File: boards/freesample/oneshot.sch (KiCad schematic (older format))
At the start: 0 parts

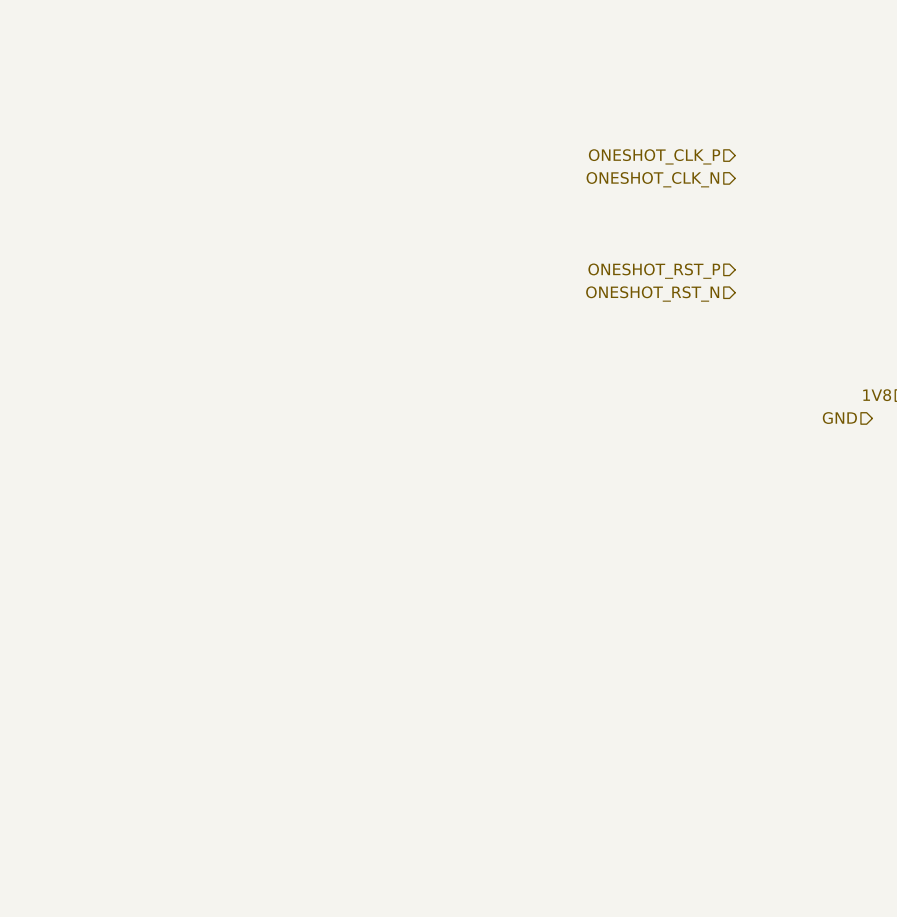
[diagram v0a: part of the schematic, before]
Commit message: Continued initial schematic capture
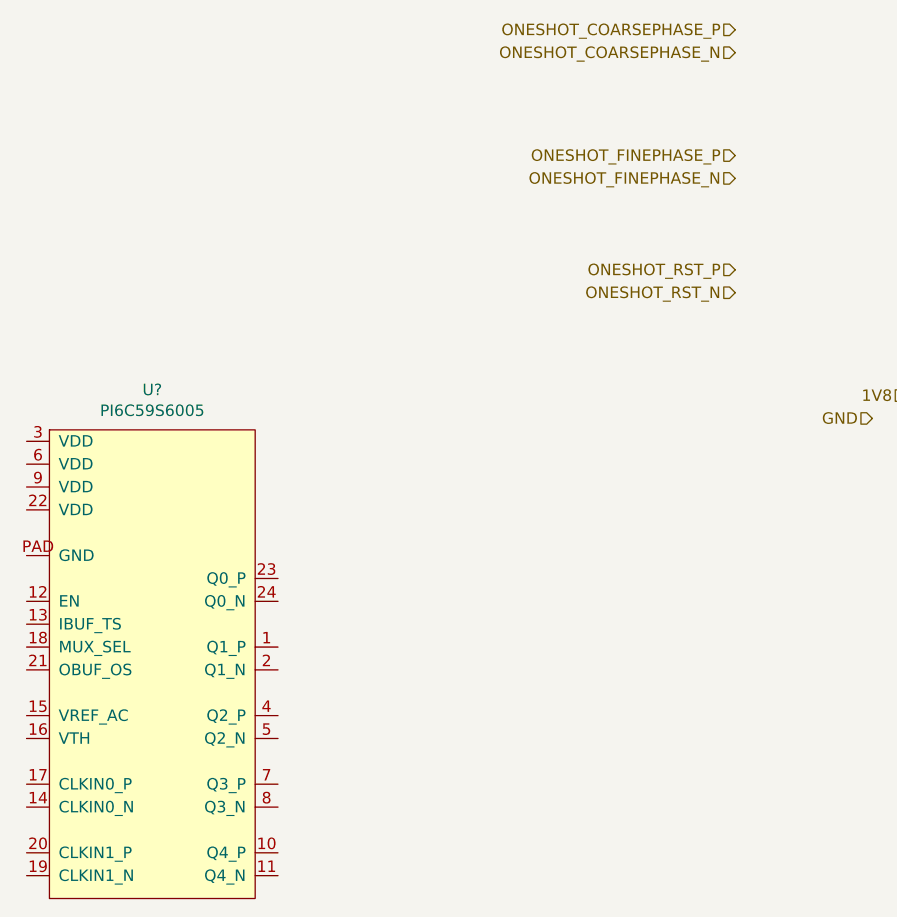
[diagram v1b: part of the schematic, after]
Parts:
- added U?: PI6C59S6005, symbol special-azonenberg:PI6C59S6005
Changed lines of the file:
@@
 $Descr A4 11693 8268
 encoding utf-8
-Sheet 6 11
+Sheet 6 12
 Title "FREESAMPLE Oscilloscope"
-Date "2018-12-15"
+Date "2018-12-17"
 Rev "0.1"
 Comp "Andrew D. Zonenberg / Antikernel Labs"
@@
 ONESHOT_RST_N
 Text HLabel 6150 2150 0    50   Input ~ 0
-ONESHOT_CLK_P
+ONESHOT_FINEPHASE_P
 Text HLabel 6150 2250 0    50   Input ~ 0
-ONESHOT_CLK_N
+ONESHOT_FINEPHASE_N
 Text HLabel 6900 3200 0    50   Input ~ 0
 1V8
@@
 Text HLabel 8450 3250 0    50   Output ~ 0
 ONESHOT_TRIGGERED_N
+$Comp
+L special-azonenberg:PI6C59S6005 U?
+U 1 1 5C3E7E97
+P 3150 5400
+F 0 "U?" H 3600 7625 50  0000 C CNN
+F 1 "PI6C59S6005" H 3600 7534 50  0000 C CNN
+F 2 "" H 3150 5100 50  0001 C CNN
+F 3 "" H 3150 5100 50  0001 C CNN
+	1    3150 5400
+	1    0    0    -1
+$EndComp
+Text HLabel 6150 1600 0    50   Input ~ 0
+ONESHOT_COARSEPHASE_P
+Text HLabel 6150 1700 0    50   Input ~ 0
+ONESHOT_COARSEPHASE_N
 $EndSCHEMATC

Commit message: Continued work on schematic capture
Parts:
- gave numbers to parts that had none: 1
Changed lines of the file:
@@
 Rev "0.1"
 Comp "Andrew D. Zonenberg / Antikernel Labs"
-Comment1 ""
+Comment1 "Digital one-shot and reset sync for ADC trigger"
 Comment2 ""
 Comment3 ""
@@
 ONESHOT_TRIGGERED_N
 $Comp
-L special-azonenberg:PI6C59S6005 U?
+L special-azonenberg:PI6C59S6005 U7
 U 1 1 5C3E7E97
 P 3150 5400
-F 0 "U?" H 3600 7625 50  0000 C CNN
+F 0 "U7" H 3600 7625 50  0000 C CNN
 F 1 "PI6C59S6005" H 3600 7534 50  0000 C CNN
 F 2 "" H 3150 5100 50  0001 C CNN

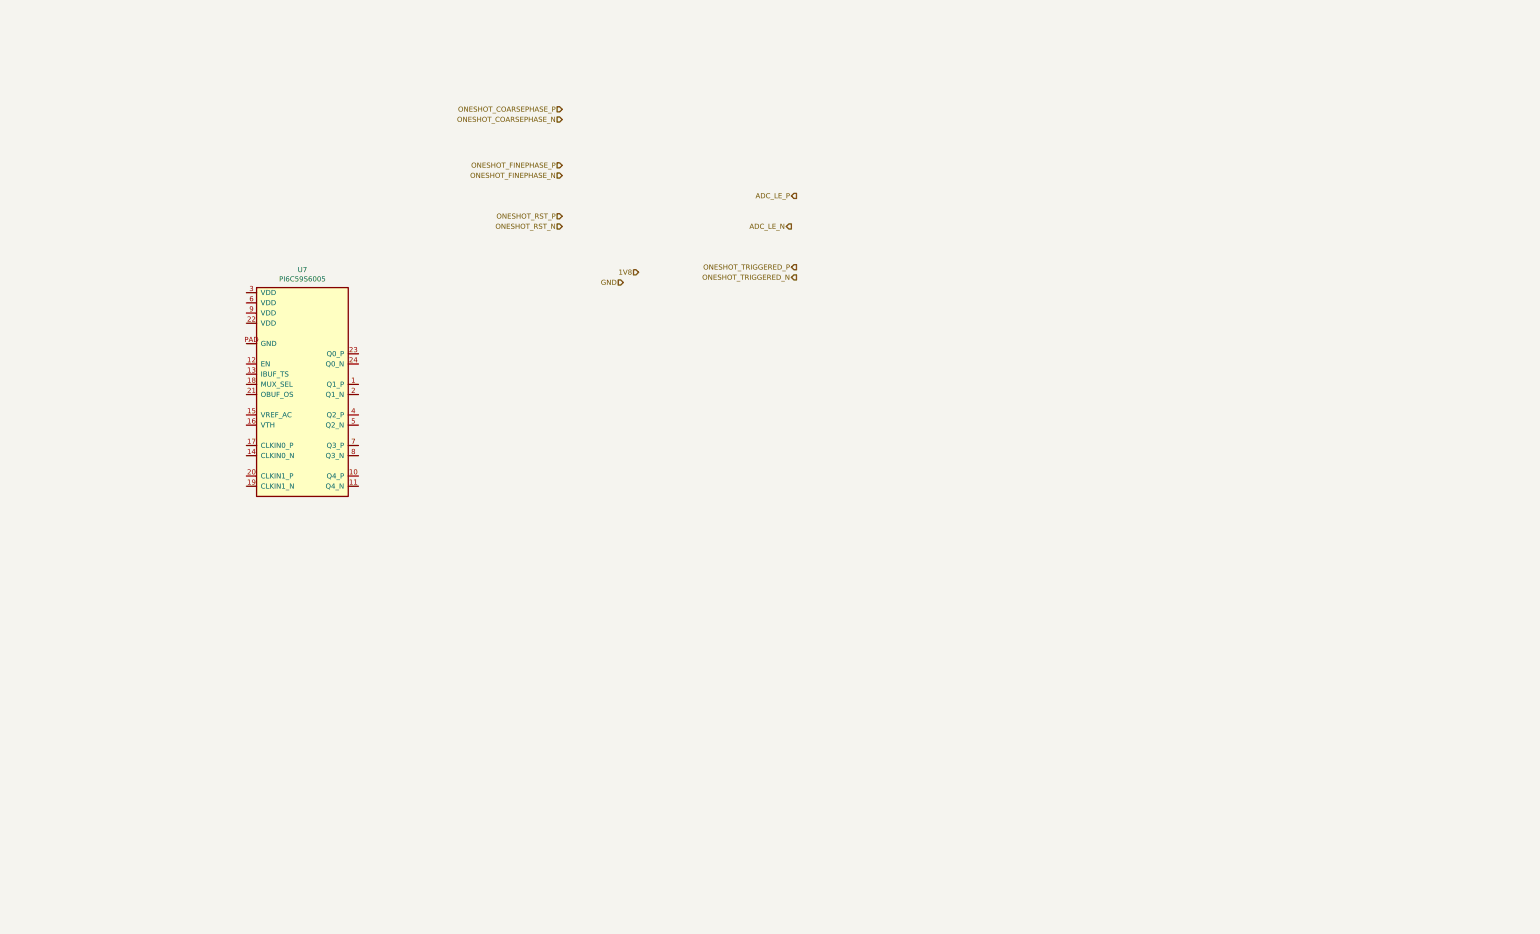
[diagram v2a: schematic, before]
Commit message: Continued work on FREESAMPLE schematic including PSU.
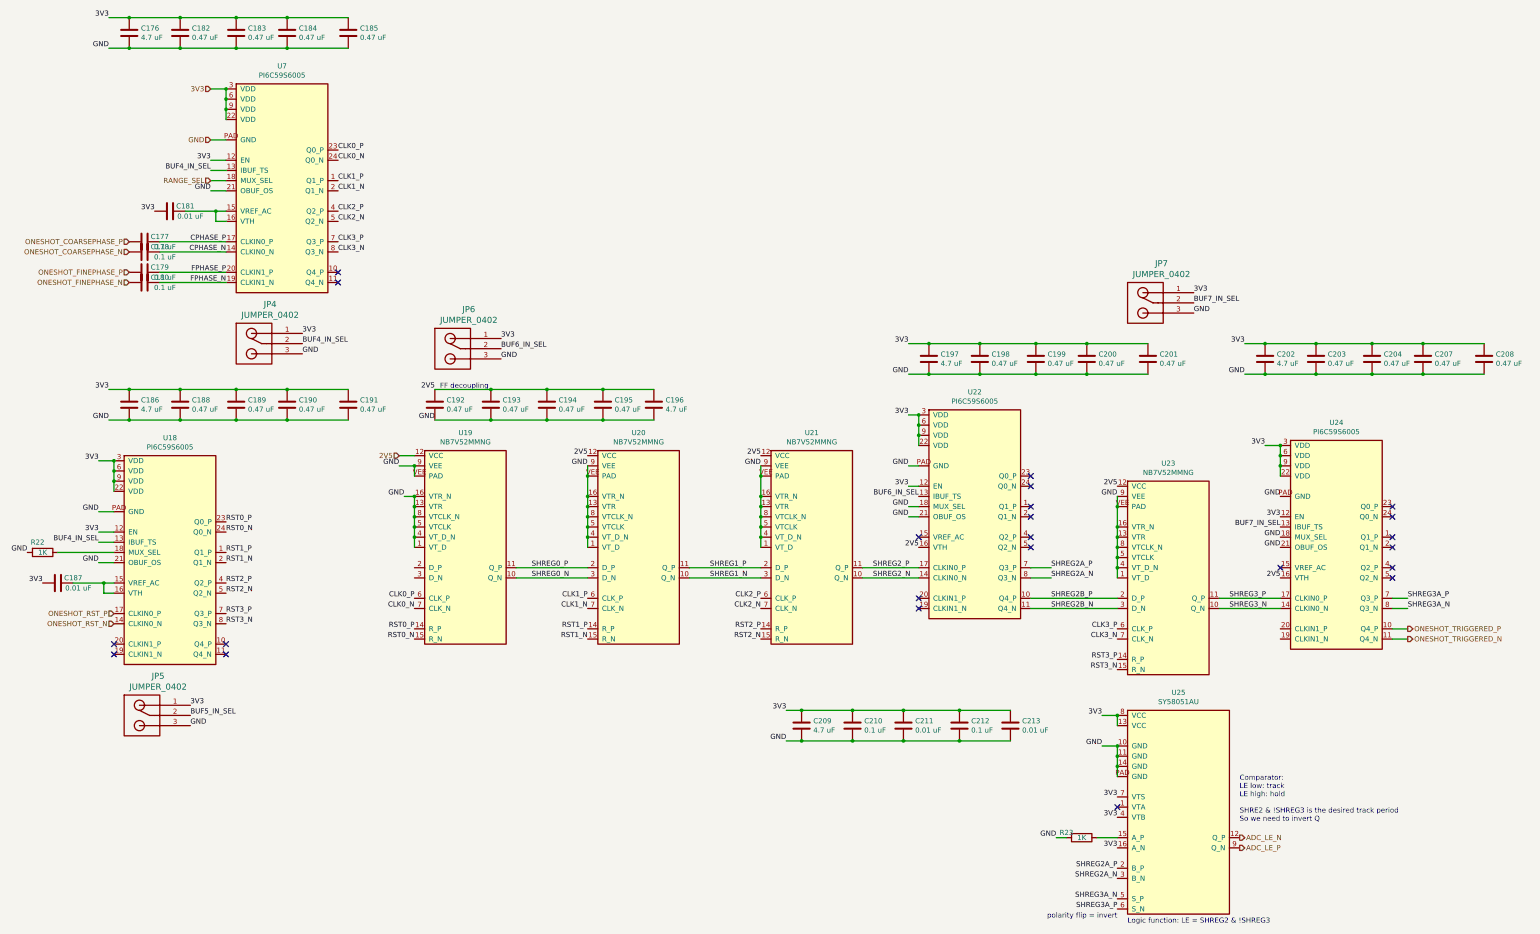
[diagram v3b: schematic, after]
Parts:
- added C176, C186, C196, C197, C202, C209: 4.7 uF, symbol device:C
- added C177, C178, C179, C180, C210, C212: 0.1 uF, symbol device:C
- added C181, C187, C211, C213: 0.01 uF, symbol device:C
- added C182, C183, C184, C185, C188, C189, C190, C191, C192, C193, C194, C195, C198, C199, C200, C201, C203, C204, C207, C208: 0.47 uF, symbol device:C
- added JP4, JP5, JP6, JP7: JUMPER_0402, symbol special-azonenberg:JUMPER_0402_SPDT
- added R22, R23: 1K, symbol device:R
- added U18, U22, U24: PI6C59S6005, symbol special-azonenberg:PI6C59S6005
- added U19, U20, U21, U23: NB7V52MMNG, symbol special-azonenberg:NB7V52MMNG
- added U25: SY58051AU, symbol special-azonenberg:SY58051AU
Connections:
- net ADC_LE_N: now also U25.12 (Q_P)
- net ADC_LE_P: now also U25.9 (Q_N)
- net GND: now also U7.21 (OBUF_OS), U7.PAD (GND), C176.2, C182.2, C183.2, C184.2, C185.2, C186.2, C188.2, C189.2, C190.2, C191.2, C192.2, C193.2, C194.2, C195.2, C196.2, C197.2, C198.2, C199.2, C200.2, C201.2, C202.2, C203.2, C204.2, C207.2, C208.2, C209.2, C210.2, C211.2, C212.2, C213.2, JP4.3, JP5.3, JP6.3, JP7.3, R22.2, R23.2, U18.21 (OBUF_OS), U18.PAD (GND), U19.1 (VT_D), U19.13 (VTR), U19.16 (VTR_N), U19.4 (VT_D_N), U19.5 (VTCLK), U19.8 (VTCLK_N), U19.9 (VEE), U19.VEE (PAD), U20.1 (VT_D), U20.13 (VTR), U20.16 (VTR_N), U20.4 (VT_D_N), U20.5 (VTCLK), U20.8 (VTCLK_N), U20.9 (VEE), U20.VEE (PAD), U21.1 (VT_D), U21.13 (VTR), U21.16 (VTR_N), U21.4 (VT_D_N), U21.5 (VTCLK), U21.8 (VTCLK_N), U21.9 (VEE), U21.VEE (PAD), U22.18 (MUX_SEL), U22.21 (OBUF_OS), U22.PAD (GND), U23.1 (VT_D), U23.13 (VTR), U23.16 (VTR_N), U23.4 (VT_D_N), U23.5 (VTCLK), U23.8 (VTCLK_N), U23.9 (VEE), U23.VEE (PAD), U24.18 (MUX_SEL), U24.21 (OBUF_OS), U24.PAD (GND), U25.10 (GND), U25.11 (GND), U25.14 (GND), U25.PAD (GND)
- net ONESHOT_COARSEPHASE_N: now also C178.2
- net ONESHOT_COARSEPHASE_P: now also C177.2
- net ONESHOT_FINEPHASE_N: now also C180.2
- net ONESHOT_FINEPHASE_P: now also C179.2
- net ONESHOT_RST_N: now also U18.14 (CLKIN0_N)
- net ONESHOT_RST_P: now also U18.17 (CLKIN0_P)
- net ONESHOT_TRIGGERED_N: now also U24.11 (Q4_N)
- net ONESHOT_TRIGGERED_P: now also U24.10 (Q4_P)
- net CLK1_P: now reaches U7.1 (Q1_P)
- net CLK1_P: now also U20.6 (CLK_P)
- net 3V3: now reaches U7.12 (EN)
- net 3V3: now also U7.22 (VDD), U7.3 (VDD), U7.6 (VDD), U7.9 (VDD), C176.1, C181.2, C182.1, C183.1, C184.1, C185.1, C186.1, C187.2, C188.1, C189.1, C190.1, C191.1, C197.1, C198.1, C199.1, C200.1, C201.1, C202.1, C203.1, C204.1, C207.1, C208.1, C209.1, C210.1, C211.1, C212.1, C213.1, JP4.1, JP5.1, JP6.1, JP7.1, U18.12 (EN), U18.22 (VDD), U18.3 (VDD), U18.6 (VDD), U18.9 (VDD), U22.12 (EN), U22.22 (VDD), U22.3 (VDD), U22.6 (VDD), U22.9 (VDD), U24.12 (EN), U24.22 (VDD), U24.3 (VDD), U24.6 (VDD), U24.9 (VDD), U25.13 (VCC), U25.16 (A_N), U25.4 (VTB), U25.7 (VTS), U25.8 (VCC)
- net BUF4_IN_SEL: now reaches U7.13 (IBUF_TS)
- net BUF4_IN_SEL: now also JP4.2, U18.13 (IBUF_TS)
- net CPHASE_N: now reaches U7.14 (CLKIN0_N)
- net CPHASE_N: now also C178.1
- net at U7.15 (VREF_AC): now also U7.16 (VTH), C181.1
- net CPHASE_P: now reaches U7.17 (CLKIN0_P)
- net CPHASE_P: now also C177.1
- net RANGE_SEL: now reaches U7.18 (MUX_SEL)
- net FPHASE_N: now reaches U7.19 (CLKIN1_N)
- net FPHASE_N: now also C180.1
- net CLK1_N: now reaches U7.2 (Q1_N)
- net CLK1_N: now also U20.7 (CLK_N)
- net FPHASE_P: now reaches U7.20 (CLKIN1_P)
- net FPHASE_P: now also C179.1
- net CLK0_P: now reaches U7.23 (Q0_P)
- net CLK0_P: now also U19.6 (CLK_P)
- net CLK0_N: now reaches U7.24 (Q0_N)
- net CLK0_N: now also U19.7 (CLK_N)
- net CLK2_P: now reaches U7.4 (Q2_P)
- net CLK2_P: now also U21.6 (CLK_P)
- net CLK2_N: now reaches U7.5 (Q2_N)
- net CLK2_N: now also U21.7 (CLK_N)
- net CLK3_P: now reaches U7.7 (Q3_P)
- net CLK3_P: now also U23.6 (CLK_P)
- net CLK3_N: now reaches U7.8 (Q3_N)
- net CLK3_N: now also U23.7 (CLK_N)
- new net: C187.1, U18.15 (VREF_AC), U18.16 (VTH)
- new net: R22.1, U18.18 (MUX_SEL)
- new net: R23.1, U25.15 (A_P)
- new net 2V5: C192.1, C193.1, C194.1, C195.1, C196.1, U19.12 (VCC), U20.12 (VCC), U21.12 (VCC), U22.16 (VTH), U23.12 (VCC), U24.16 (VTH)
- new net BUF5_IN_SEL: JP5.2
- new net BUF6_IN_SEL: JP6.2, U22.13 (IBUF_TS)
- new net BUF7_IN_SEL: JP7.2, U24.13 (IBUF_TS)
- new net RST0_N: U18.24 (Q0_N), U19.15 (R_N)
- new net RST0_P: U18.23 (Q0_P), U19.14 (R_P)
- new net RST1_N: U18.2 (Q1_N), U20.15 (R_N)
- new net RST1_P: U18.1 (Q1_P), U20.14 (R_P)
- new net RST2_N: U18.5 (Q2_N), U21.15 (R_N)
- new net RST2_P: U18.4 (Q2_P), U21.14 (R_P)
- new net RST3_N: U18.8 (Q3_N), U23.15 (R_N)
- new net RST3_P: U18.7 (Q3_P), U23.14 (R_P)
- new net SHREG0_N: U19.10 (Q_N), U20.3 (D_N)
- new net SHREG0_P: U19.11 (Q_P), U20.2 (D_P)
- new net SHREG1_N: U20.10 (Q_N), U21.3 (D_N)
- new net SHREG1_P: U20.11 (Q_P), U21.2 (D_P)
- new net SHREG2A_N: U22.8 (Q3_N), U25.3 (B_N)
- new net SHREG2A_P: U22.7 (Q3_P), U25.2 (B_P)
- new net SHREG2B_N: U22.11 (Q4_N), U23.3 (D_N)
- new net SHREG2B_P: U22.10 (Q4_P), U23.2 (D_P)
- new net SHREG2_N: U21.10 (Q_N), U22.14 (CLKIN0_N)
- new net SHREG2_P: U21.11 (Q_P), U22.17 (CLKIN0_P)
- new net SHREG3A_N: U24.8 (Q3_N), U25.5 (S_P)
- new net SHREG3A_P: U24.7 (Q3_P), U25.6 (S_N)
- new net SHREG3_N: U23.10 (Q_N), U24.14 (CLKIN0_N)
- new net SHREG3_P: U23.11 (Q_P), U24.17 (CLKIN0_P)
- no-connect marks 0 -> 23
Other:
- note added: "Comparator:\nLE low: track\nLE high: hold\n\nSHRE2 & !SHREG3 is the desired track period\nSo we need to invert Q"
- note added: "FF decoupling"
- note added: "Logic function: LE = SHREG2 & !SHREG3"
- note added: "polarity flip = invert"
- moved on the sheet: U7

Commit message: Lots more work on PSU and sch readability improvements
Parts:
- added R32: 10K, symbol device:R
- added R36: 33K, symbol device:R
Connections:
- net 2V5: now also U19.2 (D_P), R32.2
- net GND: now also R36.2; no longer U19.1 (VT_D), U19.4 (VT_D_N)
- net RST_1V9: now reaches U19.3 (D_N)
- net RST_1V9: now also R32.1, R36.1
- no-connect marks 23 -> 25
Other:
- note added: "Can't tie D_N to ground to\nget differential 1! Max\nD_P - D_N is 1200 mV"
- note added: "Fanout buffers for shift register clock/reset signals"
- note added: "Shift register for digital one-shot"
- note added: "Single-cycle pulse output for digital one-shot"
- note added: "Synchronize one-shot reset to line clock"
- moved on the sheet: C176, C177, C178, C179, C180, C181, C182, C183, C184, C185, C186, C187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

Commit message: Continued schematic capture work. Hooked up most SoM connectors.
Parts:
- added C275, C276, C277, C278, C279, C280, C281, C282, C283, C284, C285, C286, C287, C288, C289, C290, C307, C308: 0.01 uF, symbol device:C
- added C293, C294, C295, C296, C297, C298, C299, C300, C301, C302, C303, C304, C305, C306: 0.1 uF, symbol device:C
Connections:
- net 3V3: no longer C176.1, C182.1, C183.1, C184.1, C185.1, C186.1, C188.1, C189.1, C190.1, C191.1, C197.1, C198.1, C199.1, C200.1, C201.1, C202.1, C203.1, C204.1, C207.1, C208.1, C209.1, C210.1, C211.1, C212.1, C213.1, U18.22 (VDD), U18.3 (VDD), U18.6 (VDD), U18.9 (VDD), U22.22 (VDD), U22.3 (VDD), U22.6 (VDD), U22.9 (VDD), U24.22 (VDD), U24.3 (VDD), U24.6 (VDD), U24.9 (VDD), U25.13 (VCC), U25.8 (VCC), U7.22 (VDD), U7.3 (VDD), U7.6 (VDD), U7.9 (VDD)
- net CLK0_N: now also C276.1; no longer U7.24 (Q0_N)
- net CLK0_P: now also C275.1; no longer U7.23 (Q0_P)
- net CLK1_N: now also C278.1; no longer U7.2 (Q1_N)
- net CLK1_P: now also C277.1; no longer U7.1 (Q1_P)
- net CLK2_N: now also C280.1; no longer U7.5 (Q2_N)
- net CLK2_P: now also C279.1; no longer U7.4 (Q2_P)
- net CLK3_N: now also C282.1; no longer U7.8 (Q3_N)
- net CLK3_P: now also C281.1; no longer U7.7 (Q3_P)
- net ONESHOT_RST_N: now also C308.2; no longer U18.14 (CLKIN0_N)
- net ONESHOT_RST_P: now also C307.2; no longer U18.17 (CLKIN0_P)
- net RST0_N: now also C284.1; no longer U18.24 (Q0_N)
- net RST0_P: now also C283.1; no longer U18.23 (Q0_P)
- net RST1_N: now also C286.1; no longer U18.2 (Q1_N)
- net RST1_P: now also C285.1; no longer U18.1 (Q1_P)
- net RST2_N: now also C288.1; no longer U18.5 (Q2_N)
- net RST2_P: now also C287.1; no longer U18.4 (Q2_P)
- net RST3_N: now also C290.1; no longer U18.8 (Q3_N)
- net RST3_P: now also C289.1; no longer U18.7 (Q3_P)
- net SHREG0_N: now also C294.2; no longer U20.3 (D_N)
- net SHREG0_P: now also C293.2; no longer U20.2 (D_P)
- net SHREG1_N: now also C296.2; no longer U21.3 (D_N)
- net SHREG1_P: now also C295.2; no longer U21.2 (D_P)
- net SHREG2A_N: now also C302.2; no longer U25.3 (B_N)
- net SHREG2A_P: now also C301.2; no longer U25.2 (B_P)
- net SHREG2B_N: now also C300.2; no longer U23.3 (D_N)
- net SHREG2B_P: now also C299.2; no longer U23.2 (D_P)
- net SHREG2_N: now also C298.2; no longer U22.14 (CLKIN0_N)
- net SHREG2_P: now also C297.2; no longer U22.17 (CLKIN0_P)
- net SHREG3A_N: now also C303.2; no longer U25.5 (S_P)
- net SHREG3A_P: now also C304.2; no longer U25.6 (S_N)
- net SHREG3_N: now also C306.2; no longer U24.14 (CLKIN0_N)
- net SHREG3_P: now also C305.2; no longer U24.17 (CLKIN0_P)
- new net 3V3_CLKBUF: C176.1, C182.1, C183.1, C184.1, C185.1, C186.1, C188.1, C189.1, C190.1, C191.1, C197.1, C198.1, C199.1, C200.1, C201.1, C202.1, C203.1, C204.1, C207.1, C208.1, C209.1, C210.1, C211.1, C212.1, C213.1, U18.22 (VDD), U18.3 (VDD), U18.6 (VDD), U18.9 (VDD), U22.22 (VDD), U22.3 (VDD), U22.6 (VDD), U22.9 (VDD), U24.22 (VDD), U24.3 (VDD), U24.6 (VDD), U24.9 (VDD), U25.13 (VCC), U25.8 (VCC), U7.22 (VDD), U7.3 (VDD), U7.6 (VDD), U7.9 (VDD)
- new net CLK0_AC_N: C276.2, U7.24 (Q0_N)
- new net CLK0_AC_P: C275.2, U7.23 (Q0_P)
- new net CLK1_AC_N: C278.2, U7.2 (Q1_N)
- new net CLK1_AC_P: C277.2, U7.1 (Q1_P)
- new net CLK2_AC_N: C280.2, U7.5 (Q2_N)
- new net CLK2_AC_P: C279.2, U7.4 (Q2_P)
- new net CLK3_AC_N: C282.2, U7.8 (Q3_N)
- new net CLK3_AC_P: C281.2, U7.7 (Q3_P)
- new net ORST_AC_N: C308.1, U18.14 (CLKIN0_N)
- new net ORST_AC_P: C307.1, U18.17 (CLKIN0_P)
- new net RST0_AC_N: C284.2, U18.24 (Q0_N)
- new net RST0_AC_P: C283.2, U18.23 (Q0_P)
- new net RST1_AC_N: C286.2, U18.2 (Q1_N)
- new net RST1_AC_P: C285.2, U18.1 (Q1_P)
- new net RST2_AC_N: C288.2, U18.5 (Q2_N)
- new net RST2_AC_P: C287.2, U18.4 (Q2_P)
- new net RST3_AC_N: C290.2, U18.8 (Q3_N)
- new net RST3_AC_P: C289.2, U18.7 (Q3_P)
- new net SH0_AC_N: C294.1, U20.3 (D_N)
- new net SH0_AC_P: C293.1, U20.2 (D_P)
- new net SH1_AC_N: C296.1, U21.3 (D_N)
- new net SH1_AC_P: C295.1, U21.2 (D_P)
- new net SH2A_AC_N: C302.1, U25.3 (B_N)
- new net SH2A_AC_P: C301.1, U25.2 (B_P)
- new net SH2B_AC_N: C300.1, U23.3 (D_N)
- new net SH2B_AC_P: C299.1, U23.2 (D_P)
- new net SH2_AC_N: C298.1, U22.14 (CLKIN0_N)
- new net SH2_AC_P: C297.1, U22.17 (CLKIN0_P)
- new net SH3A_AC_N: C304.1, U25.6 (S_N)
- new net SH3A_AC_P: C303.1, U25.5 (S_P)
- new net SH3_AC_N: C306.1, U24.14 (CLKIN0_N)
- new net SH3_AC_P: C305.1, U24.17 (CLKIN0_P)
- no-connect marks 25 -> 27
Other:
- moved on the sheet: C176, C177, C178, C179, C180, C181, C182, C183, C184, C185, C186, C187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

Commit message: Lots of ERC fixes, added CML-to-LVDS buffers for FPGA input signals
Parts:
- added C311: 0.47 uF, symbol device:C
- added U40: DS25BR150, symbol special-azonenberg:DS25BR150
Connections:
- net 3V3_CLKBUF: now also C311.2, U40.8 (VCC)
- net BUF4_IN_SEL: no longer U18.13 (IBUF_TS)
- net BUF5_IN_SEL: now also U18.13 (IBUF_TS)
- net GND: now also C311.1, U40.PAD (VSS)
- net ONESHOT_TRIGGERED_N: now also U40.6 (OUT_N); no longer U24.11 (Q4_N)
- net ONESHOT_TRIGGERED_P: now also U40.7 (OUT_P); no longer U24.10 (Q4_P)
- new net TRIG_N: U24.11 (Q4_N), U40.3 (IN_N)
- new net TRIG_P: U24.10 (Q4_P), U40.2 (IN_P)
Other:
- note added: "CML-to-LVDS buffer for FPGA input"
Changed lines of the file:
@@
 Text HLabel 2550 6750 0    50   Input ~ 0
 GND
-Text HLabel 14850 3550 2    50   Output ~ 0
+Text HLabel 2750 10050 2    50   Output ~ 0
 ONESHOT_TRIGGERED_P
-Text HLabel 14850 3650 2    50   Output ~ 0
+Text HLabel 2750 10150 2    50   Output ~ 0
 ONESHOT_TRIGGERED_N
 $Comp
@@
 GND
 Text Label 6350 7050 2    50   ~ 0
-BUF4_IN_SEL
+BUF5_IN_SEL
 Wire Wire Line
 	6350 7050 6500 7050
@@
 Wire Wire Line
 	3650 3350 4050 3350
+$Comp
+L special-azonenberg:DS25BR150 U40
+U 1 1 5D0E82CB
+P 1550 10300
+F 0 "U40" H 2000 11097 60  0000 C CNN
+F 1 "DS25BR150" H 2000 10991 60  0000 C CNN
+F 2 "" H 1550 10300 60  0001 C CNN
+F 3 "" H 1550 10300 60  0001 C CNN
+	1    1550 10300
+	1    0    0    -1
+$EndComp
+Text Label 14850 3550 0    50   ~ 0
+TRIG_P
+Text Label 14850 3650 0    50   ~ 0
+TRIG_N
+Text Label 1250 10050 2    50   ~ 0
+TRIG_P
+Text Label 1250 10150 2    50   ~ 0
+TRIG_N
+Text Notes 550  11100 0    98   ~ 0
+CML-to-LVDS buffer for FPGA input
+Text Label 1050 9750 2    50   ~ 0
+3V3_CLKBUF
+Text Label 1250 9850 2    50   ~ 0
+GND
+$Comp
+L device:C C311
+U 1 1 5D14811F
+P 1050 9600
+F 0 "C311" H 1165 9646 50  0000 L CNN
+F 1 "0.47 uF" H 1165 9555 50  0000 L CNN
+F 2 "" H 1088 9450 50  0001 C CNN
+F 3 "" H 1050 9600 50  0001 C CNN
+	1    1050 9600
+	1    0    0    -1
+$EndComp
+Wire Wire Line
+	1050 9750 1250 9750
+Text Label 1050 9450 2    50   ~ 0
+GND
 $EndSCHEMATC
